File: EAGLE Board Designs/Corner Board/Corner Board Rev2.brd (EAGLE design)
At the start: 100 x 50 mm, 44 parts, among them J1 CONNECTOR-8_AMPHENOL_M12A_08P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, J2 CONNECTOR-2_MICROFIT_SMD_RIGH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, J3 CONNECTOR-8_AMPHENOL_M12A_08P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, J4 CONNECTOR-4_μF_S_RA_, J5 CONNECTOR-4_μF_S_RA_, U1 VOLTAGE_REGULATOR_SOT-89_15V, U2 OPAMP_1_CHANNEL_OPA991, U3 INA823DT, U4 OPAMP_1_CHANNEL_OPA991, U5 OPAMP_1_CHANNEL_OPA991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

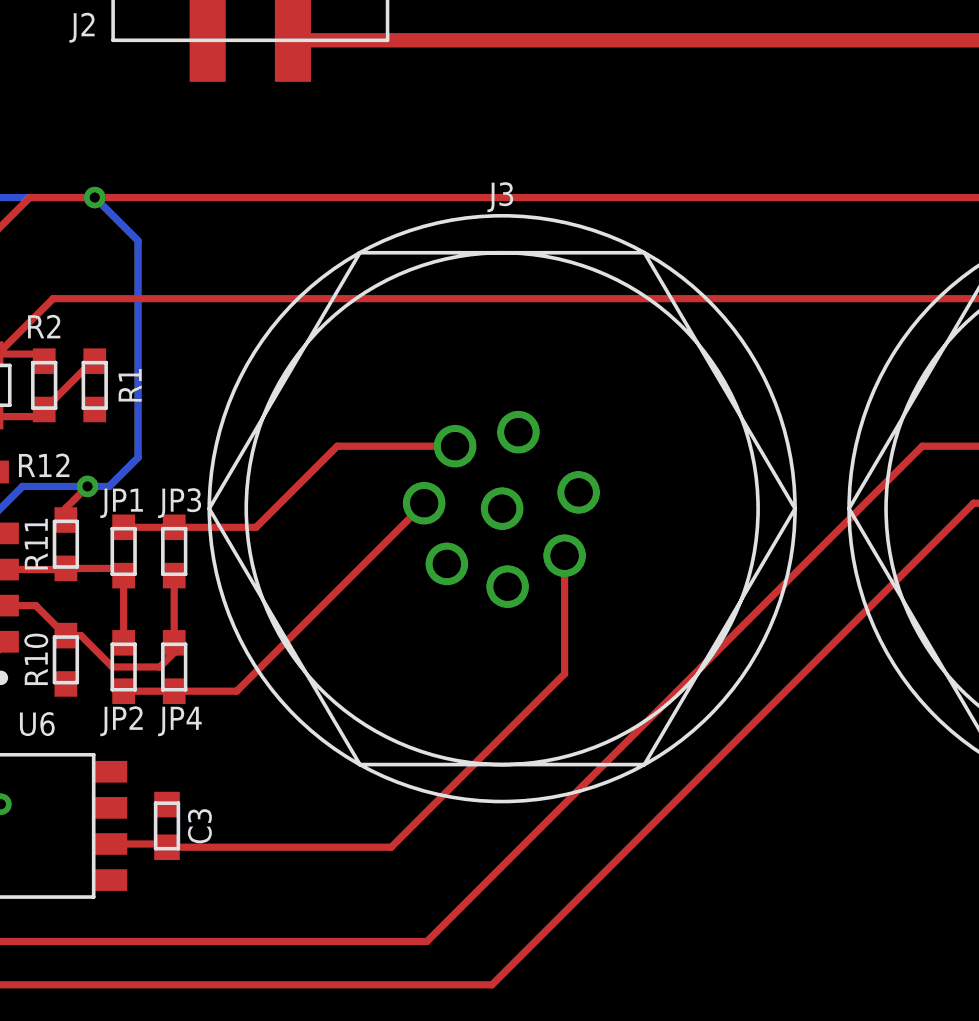
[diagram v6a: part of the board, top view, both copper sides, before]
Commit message: updated load cell connector
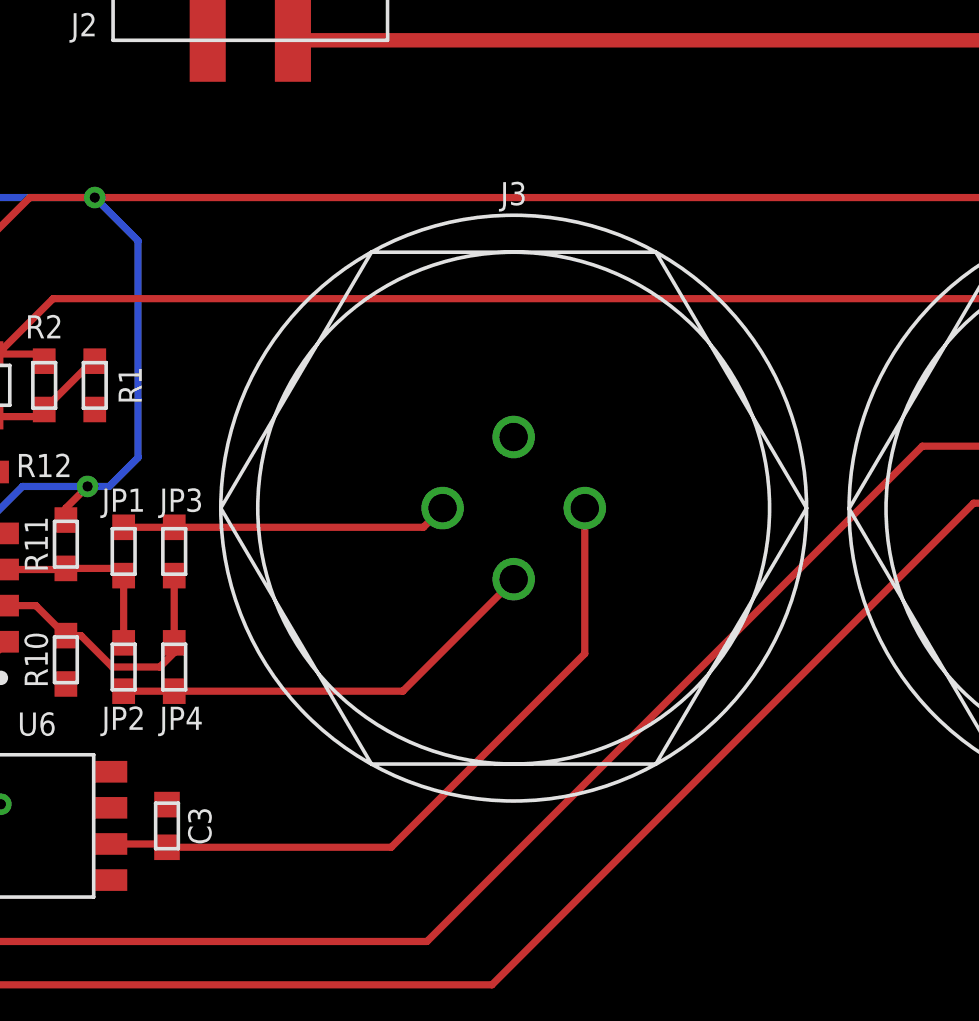
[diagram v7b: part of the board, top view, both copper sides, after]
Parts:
- J3: value CONNECTOR-8_AMPHENOL_M12A_08PMMP_ -> CONNECTOR-4_AMPHENOL_M12A_04PMMP_; device HyTechDevices:M12A-08PMMP -> HyTechDevices:M12A-04PMMP
- moved J3 0.41 mm to (64.3, 23.1)
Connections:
- net 10V: now also J3.1; no longer J3.7
- net GND: now also J3.2; no longer J3.8
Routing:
- net SIGNAL-: track 13.3 -> 15.4 mm
- net 10V: track 22.7 -> 24.6 mm
- net SIGNAL+: track 12.8 -> 11.5 mm
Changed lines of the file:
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@@
 <drawing>
 <settings>
-<setting alwaysvectorfont="yes"/>
+<setting alwaysvectorfont="no"/>
 <setting verticaltext="up"/>
 </settings>
-<grid distance="10" unitdist="mil" unit="mil" style="lines" multiple="1" display="no" altdistance="5" altunitdist="mil" altunit="mil"/>
+<grid distance="10" unitdist="mil" unit="mil" style="lines" multiple="1" display="yes" altdistance="5" altunitdist="mil" altunit="mil"/>
 <layers>
 <layer number="1" name="Top" color="4" fill="1" visible="yes" active="yes"/>
@@
 <attribute name="NAME" x="86.357" y="33.747" size="0.8128" layer="25" font="vector" align="bottom-center"/>
 </element>
-<element name="J3" library="HyTechDevices" package="M12A-08PMMP" value="CONNECTOR-8_AMPHENOL_M12A_08PMMP_" x="63.857" y="23.095" smashed="yes">
-<attribute name="DKPN" value="1754-1026-ND" x="63.857" y="23.095" size="1.778" layer="27" display="off"/>
-<attribute name="MANUFACTURER" value="Amphenol LTW" x="63.857" y="23.095" size="1.778" layer="27" display="off"/>
-<attribute name="MOPN" value="523-M12A08PMMPSF8001" x="63.857" y="23.095" size="1.778" layer="27" display="off"/>
-<attribute name="MPN" value="M12A-08PMMP-SF8001" x="63.857" y="23.095" size="1.778" layer="27" display="off"/>
-<attribute name="NAME" x="63.857" y="33.747" size="0.8128" layer="25" font="vector" align="bottom-center"/>
-</element>
 <element name="U4" library="HyTechDevices" package="SC-70-5" value="OPAMP_1_CHANNEL_OPA991" x="26.162" y="27.686" smashed="yes" rot="R180">
 <attribute name="DKPN" value="296-OPA991IDCKRCT-ND" x="26.162" y="27.686" size="1.778" layer="27" rot="R180" display="off"/>
@@
 <attribute name="VOLTAGE" value="50V" x="20.066" y="29.21" size="1.778" layer="27" rot="R270" display="off"/>
 </element>
+<element name="J3" library="HyTechDevices" package="M12A-04PMMP" value="CONNECTOR-4_AMPHENOL_M12A_04PMMP_" x="64.262" y="23.114" smashed="yes">
+<attribute name="DKPN" value="1754-1007-ND " x="64.262" y="23.114" size="1.778" layer="27" display="off"/>
+<attribute name="MANUFACTURER" value="Amphenol" x="64.262" y="23.114" size="1.778" layer="27" display="off"/>
+<attribute name="MPN" value="M12A-04PMMP-SF8001" x="64.262" y="23.114" size="1.778" layer="27" display="off"/>
+<attribute name="NAME" x="64.262" y="33.766" size="0.8128" layer="25" font="vector" align="bottom-center"/>
+</element>
 </elements>
 <signals>
@@
 <wire x1="51.955" y1="11.303" x2="52.07" y2="11.188" width="0.254" layer="1"/>
 <wire x1="52.07" y1="11.188" x2="59.956" y2="11.188" width="0.254" layer="1"/>
-<contactref element="J3" pad="7"/>
-<wire x1="59.956" y1="11.188" x2="66.053246875" y2="17.285246875" width="0.254" layer="1"/>
-<wire x1="66.053246875" y1="17.285246875" x2="66.053246875" y2="21.440009375" width="0.254" layer="1"/>
+<contactref element="J3" pad="1"/>
+<wire x1="66.762" y1="17.994" x2="66.762" y2="23.114" width="0.254" layer="1"/>
+<wire x1="59.956" y1="11.188" x2="66.762" y2="17.994" width="0.254" layer="1"/>
 </signal>
 <signal name="GND">
@@
 <contactref element="C3" pad="2"/>
 <contactref element="J1" pad="8"/>
-<contactref element="J3" pad="8"/>
 <contactref element="U5" pad="2"/>
 <contactref element="C4" pad="2"/>
@@
 <contactref element="C6" pad="2"/>
 <contactref element="C7" pad="2"/>
+<contactref element="J3" pad="2"/>
 </signal>
 <signal name="SIGNAL+">
@@
 <wire x1="50.546" y1="22.44" x2="52.324" y2="22.44" width="0.254" layer="1"/>
 <contactref element="J3" pad="3"/>
-<wire x1="52.324" y1="22.44" x2="55.206" y2="22.44" width="0.254" layer="1"/>
-<wire x1="62.202009375" y1="25.291246875" x2="58.057246875" y2="25.291246875" width="0.254" layer="1"/>
-<wire x1="58.057246875" y1="25.291246875" x2="55.206" y2="22.44" width="0.254" layer="1"/>
+<wire x1="61.088" y1="22.44" x2="61.762" y2="23.114" width="0.254" layer="1"/>
+<wire x1="52.324" y1="22.44" x2="61.088" y2="22.44" width="0.254" layer="1"/>
 </signal>
 <signal name="SIGNAL-">
@@
 <contactref element="JP4" pad="2"/>
 <wire x1="50.546" y1="16.676" x2="52.324" y2="16.676" width="0.254" layer="1"/>
-<wire x1="52.324" y1="16.676" x2="54.522" y2="16.676" width="0.254" layer="1"/>
+<wire x1="52.324" y1="16.676" x2="60.364" y2="16.676" width="0.254" layer="1"/>
 <contactref element="J3" pad="4"/>
-<wire x1="54.522" y1="16.676" x2="61.1137" y2="23.2677" width="0.254" layer="1"/>
-<wire x1="61.1137" y1="23.28683125" x2="61.1137" y2="23.2677" width="0.254" layer="1"/>
+<wire x1="60.364" y1="16.676" x2="64.262" y2="20.574" width="0.254" layer="1"/>
+<wire x1="64.262" y1="20.574" x2="64.262" y2="20.614" width="0.254" layer="1"/>
 </signal>
 <signal name="PREINTERLOCK">

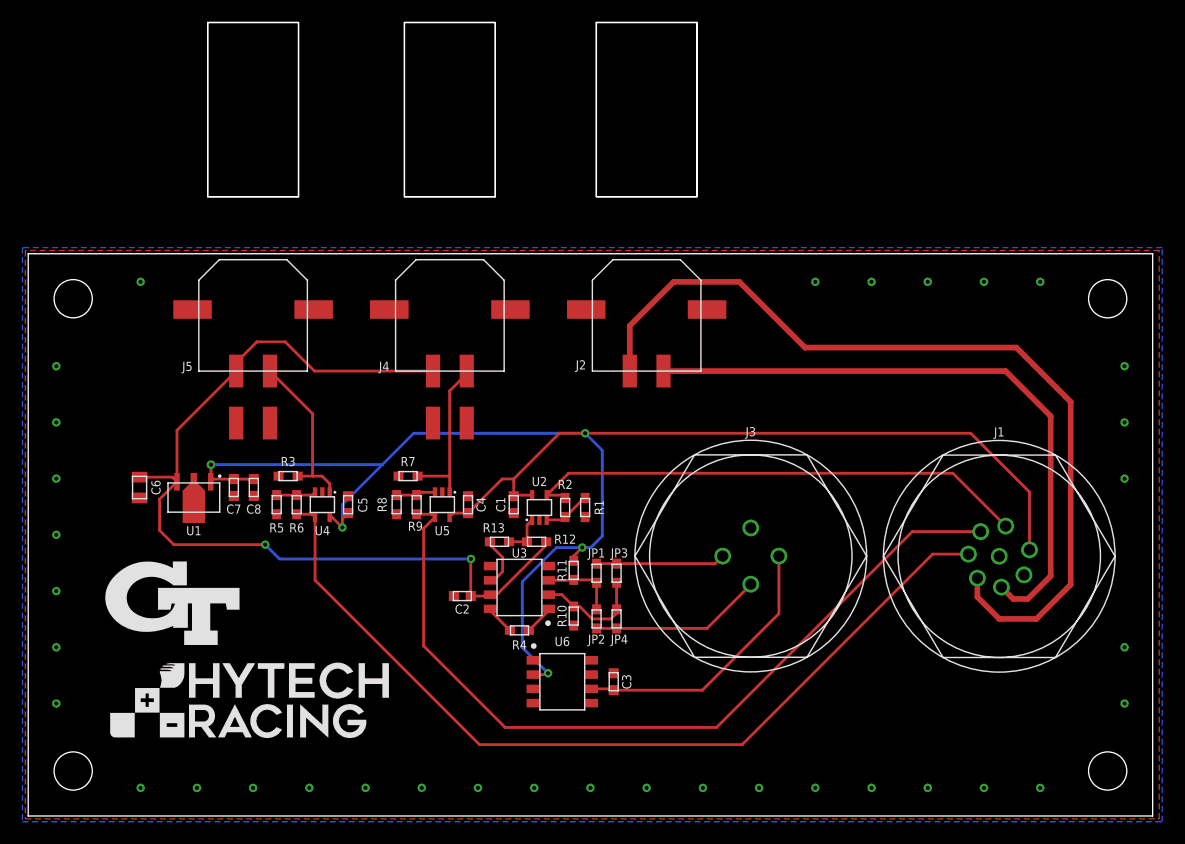
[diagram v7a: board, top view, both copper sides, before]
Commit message: changed suspot gain. cleaned up schema. passed DRC.
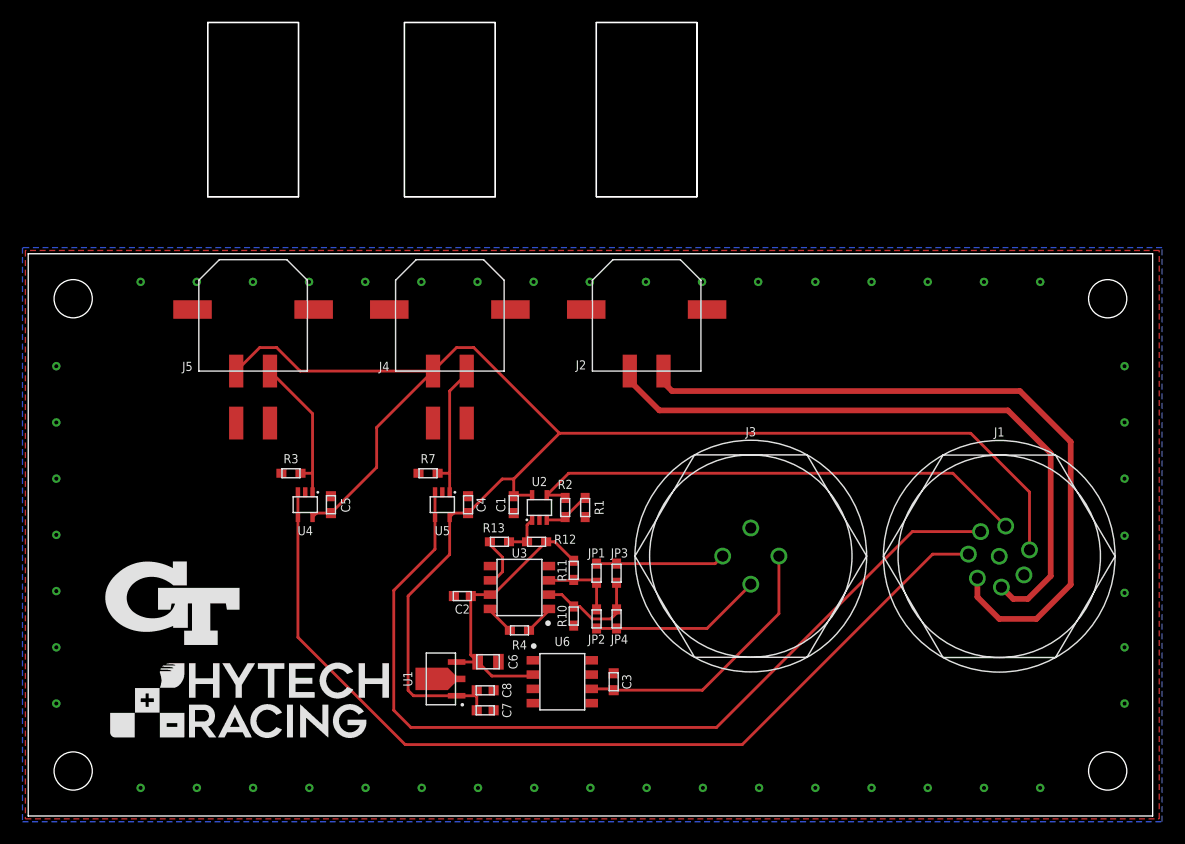
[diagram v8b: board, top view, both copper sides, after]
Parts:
- removed R5, R8: RESISTOR_0603_2.74K, HyTechDevices:0603-RES
- removed R6, R9: RESISTOR_0603_10.5K, HyTechDevices:0603-RES
- moved C6 34.6 mm to (40.9, 13.7), turned to 0 degrees
- moved C7 29.9 mm to (40.6, 9.40), turned to 0 degrees
- moved U1 29.2 mm to (38.1, 12.2), turned to 90 degrees
- moved C8 27.4 mm to (40.6, 11.2), turned to 0 degrees
- moved R7 1.80 mm to (35.6, 30.5)
- moved C5 1.52 mm to (26.9, 27.7)
- moved U4 1.52 mm to (24.6, 27.7)
- moved R3 0.36 mm to (23.4, 30.5)
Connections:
- removed net N$5: R5.2, R6.1, U4.3
- removed net N$8: R8.2, R9.1, U5.3
- net +24V: now also J4.1, J5.1; no longer R11.2, U6.2
- net 15V: now also R11.2, U6.2; no longer J4.1, J5.1
- net GND: no longer R5.1, R8.1
- net POSTINTERLOCK: now also J2.1; no longer J2.2
- net PREINTERLOCK: now also J2.2; no longer J2.1
- net SUS_POT_1_24V: now also U5.3; no longer R9.2
- net SUS_POT_2_24V: now also U4.3; no longer R6.2
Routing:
- net 15V: track 81.5 -> 25.3 mm, vias 2 -> 0
- net PREINTERLOCK: track 77.6 -> 64.2 mm
- net SUS_POT_1_24V: track 73.4 -> 80.9 mm
- net SUS_POT_2_24V: track 78.5 -> 83.5 mm
- net N$8: track 3.52 -> 0.00 mm
- net N$5: track 3.52 -> 0.00 mm
- net +24V: track 145.7 -> 142.9 mm, vias 5 -> 0
- net SUS_POT_1: track 14.3 -> 12.5 mm
- net POSTINTERLOCK: track 56.0 -> 57.5 mm
- net SUS_POT_2: track 14.8 -> 13.4 mm
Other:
- board text added: "Corner Board rev2 Designed by: Liwei Sun Shayan Noorani Mikhail Allen Brendan Bassett"
- board text removed: "Corner Board rev2 Designed by: Liwei Sun Shayan Noorani Mikhail Allen"
